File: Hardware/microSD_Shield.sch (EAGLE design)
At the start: 23 parts, among them J1 AVR_SPI_PRG_6NS, U1 USD-SOCKETNEW, U2 ARDUINO_R3_SHIELDNOLABELS, U3 HEX_CONVERTER

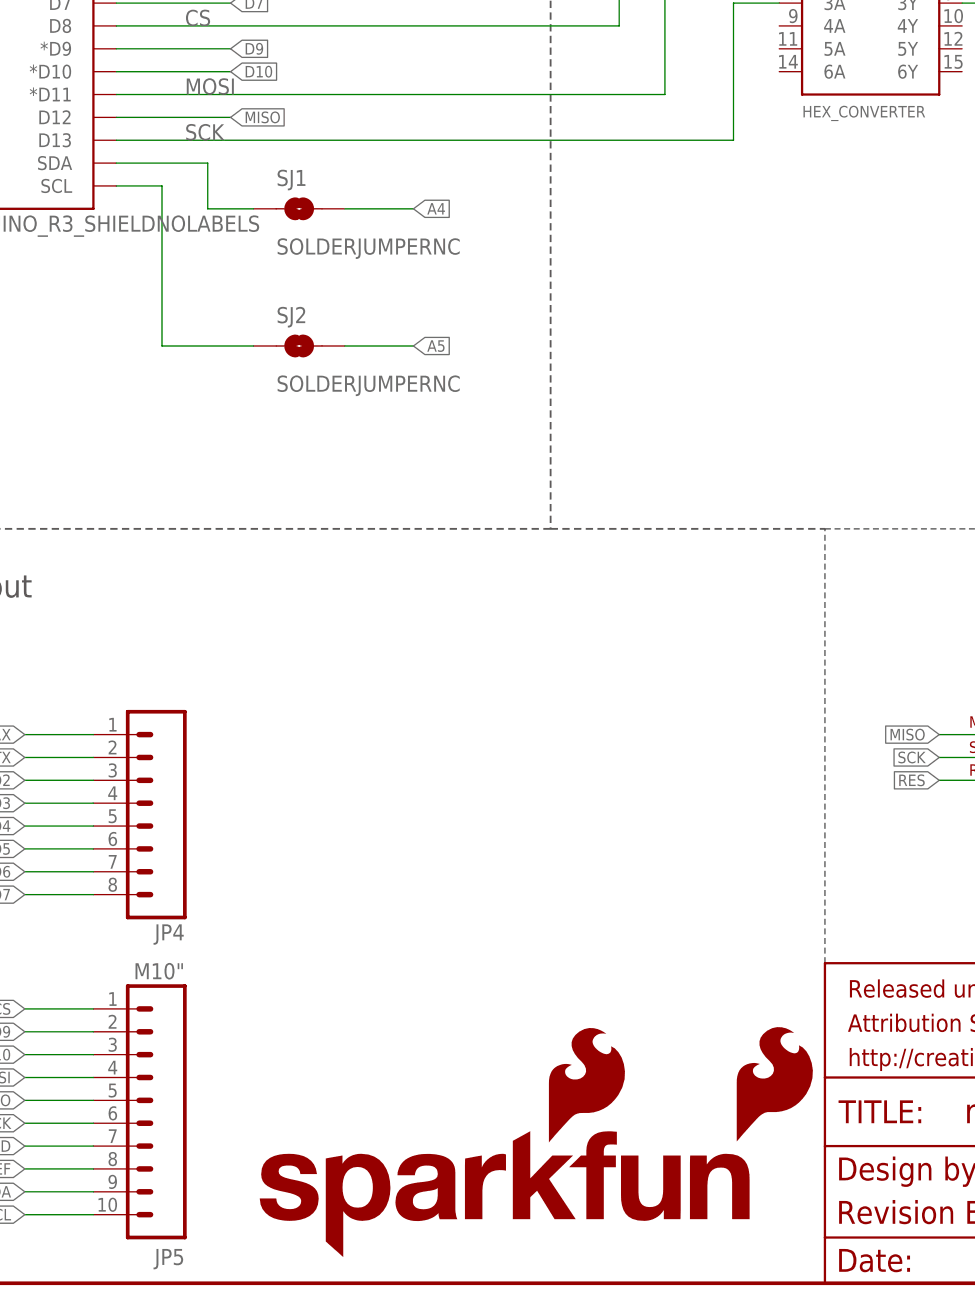
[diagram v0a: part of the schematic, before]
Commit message: Upping back flame size
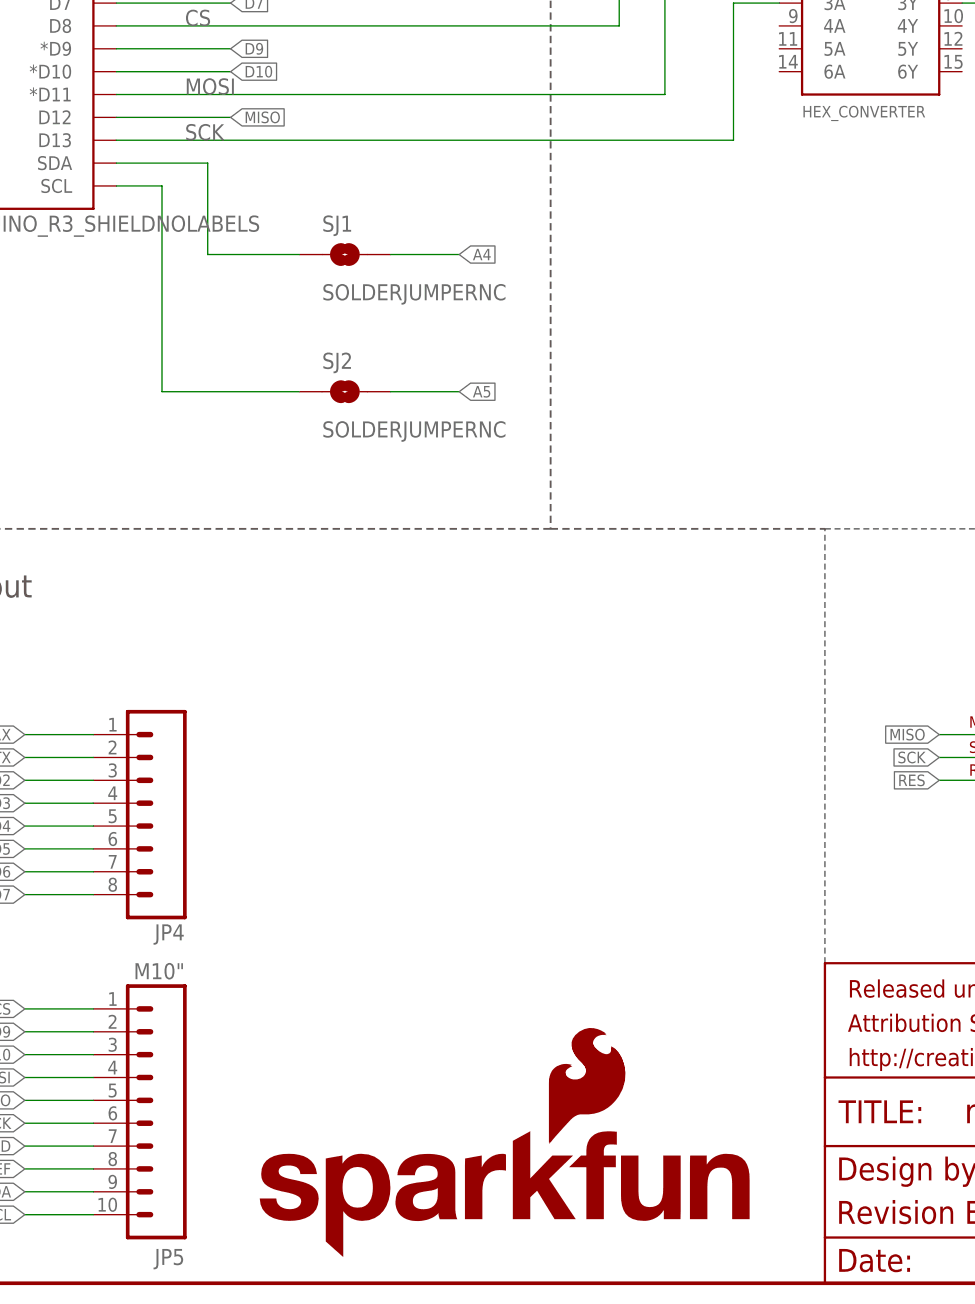
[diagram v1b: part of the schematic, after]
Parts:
- LOGO2: value SFE_LOGO_FLAME.1_INCH -> SFE_LOGO_FLAME.6_INCH; device SparkFun-Aesthetics:SFE_LOGO_FLAME.1_INCH -> SparkFun-Aesthetics:SFE_LOGO_FLAME.6_INCH
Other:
- moved on the sheet: SJ1, SJ2
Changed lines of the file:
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@@
 <part name="P+6" library="SparkFun" deviceset="3.3V" device=""/>
 <part name="P+7" library="SparkFun" deviceset="3.3V" device=""/>
-<part name="LOGO2" library="SparkFun-Aesthetics" deviceset="SFE_LOGO_FLAME" device=".1_INCH"/>
+<part name="LOGO2" library="SparkFun-Aesthetics" deviceset="SFE_LOGO_FLAME" device=".6_INCH" value="SFE_LOGO_FLAME.6_INCH"/>
 </parts>
 <sheets>
@@
 <instance part="U$1" gate="G$1" x="148.59" y="6.604"/>
 <instance part="LOGO1" gate="G$1" x="236.22" y="27.94"/>
-<instance part="SJ1" gate="1" x="88.9" y="119.38"/>
-<instance part="SJ2" gate="1" x="88.9" y="104.14"/>
+<instance part="SJ1" gate="1" x="93.98" y="114.3"/>
+<instance part="SJ2" gate="1" x="93.98" y="99.06"/>
 <instance part="J1" gate="G$1" x="175.26" y="58.42"/>
 <instance part="C1" gate="G$1" x="236.22" y="139.7"/>
@@
 <instance part="P+6" gate="G$1" x="175.26" y="106.68"/>
 <instance part="P+7" gate="G$1" x="236.22" y="147.32"/>
-<instance part="LOGO2" gate="G$1" x="137.16" y="15.24"/>
+<instance part="LOGO2" gate="G$1" x="116.332" y="14.986"/>
 </instances>
 <busses>
@@
 <segment>
 <pinref part="SJ1" gate="1" pin="2"/>
-<wire x1="93.98" y1="119.38" x2="101.6" y2="119.38" width="0.1524" layer="91"/>
-<label x="101.6" y="119.38" size="1.27" layer="95" font="vector" xref="yes"/>
+<wire x1="99.06" y1="114.3" x2="106.68" y2="114.3" width="0.1524" layer="91"/>
+<label x="106.68" y="114.3" size="1.27" layer="95" font="vector" xref="yes"/>
 </segment>
 </net>
@@
 <segment>
 <pinref part="SJ2" gate="1" pin="2"/>
-<wire x1="93.98" y1="104.14" x2="101.6" y2="104.14" width="0.1524" layer="91"/>
-<label x="101.6" y="104.14" size="1.27" layer="95" font="vector" xref="yes"/>
+<wire x1="99.06" y1="99.06" x2="106.68" y2="99.06" width="0.1524" layer="91"/>
+<label x="106.68" y="99.06" size="1.27" layer="95" font="vector" xref="yes"/>
 </segment>
 </net>
@@
 <pinref part="U2" gate="G$1" pin="SDA"/>
 <wire x1="68.58" y1="124.46" x2="78.74" y2="124.46" width="0.1524" layer="91"/>
-<wire x1="78.74" y1="124.46" x2="78.74" y2="119.38" width="0.1524" layer="91"/>
-<wire x1="78.74" y1="119.38" x2="83.82" y2="119.38" width="0.1524" layer="91"/>
+<wire x1="78.74" y1="124.46" x2="78.74" y2="114.3" width="0.1524" layer="91"/>
+<wire x1="78.74" y1="114.3" x2="88.9" y2="114.3" width="0.1524" layer="91"/>
 <pinref part="SJ1" gate="1" pin="1"/>
 </segment>
@@
 <pinref part="U2" gate="G$1" pin="SCL"/>
 <wire x1="68.58" y1="121.92" x2="73.66" y2="121.92" width="0.1524" layer="91"/>
-<wire x1="73.66" y1="121.92" x2="73.66" y2="104.14" width="0.1524" layer="91"/>
-<wire x1="73.66" y1="104.14" x2="83.82" y2="104.14" width="0.1524" layer="91"/>
+<wire x1="73.66" y1="121.92" x2="73.66" y2="99.06" width="0.1524" layer="91"/>
+<wire x1="73.66" y1="99.06" x2="88.9" y2="99.06" width="0.1524" layer="91"/>
 <pinref part="SJ2" gate="1" pin="1"/>
 </segment>
